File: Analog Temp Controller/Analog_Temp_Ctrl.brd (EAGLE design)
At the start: 100 x 59 mm, 110 parts, among them IC1 TL074D, IC3 LMV358MMX, IC4 ADA4522-2, J1 USB_MINI-B_SMT, Q1 TIP41C, T1 2N3904, T2 2N3906, U1 ADR01BRZ, U2 ATMEGA32U4-AU, U3 CJT1117-3.3-SOT223, U4 CJT1117-5.0-SOT223, U5 AD5272BRMZ-20, X1 CRYSTAL-3.2-2.5

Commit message: Completed Temperature Controller, Rdy for Mfg.
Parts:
- removed LED4: (no value), led:CHIPLED_0805
- removed U5: AD5272BRMZ-20, Analog Devices_By_element14_Batch_1:SOP50P490X110-10N
- added C27, C29, C32, C34, C35, C36, C37: 0.1uF, rcl:C0805
- added C28, C30, C33: 10uF, rcl:C0805
- added C31: 1uF, rcl:C0805
- added PWR: (no value), led:CHIPLED_0805
- added RADD: Radd, rcl:R0805
- added U6: AD5292BRUZ-20, Analog Devices_By_element14_Batch_1:SOP65P640X120-14N
- moved C9 8.41 mm to (91.2, 34.3), turned to 270 degrees
- moved R32 7.27 mm to (85.0, 30.0)
- moved R31 7.03 mm to (85.0, 27.7)
- moved C10 6.79 mm to (85.0, 25.4)
- moved C19 5.82 mm to (55.0, 46.6), turned to 180 degrees
- moved U1 4.02 mm to (90.2, 27.9), turned to 270 degrees
- moved R8 3.32 mm to (56.4, 24.3), turned to 270 degrees
- moved JP7 3.09 mm to (74.7, 25.7), turned to 180 degrees
- moved R36 2.51 mm to (59.2, 43.7), turned to 0 degrees
- moved C6 1.40 mm to (65.5, 22.1)
- moved R20 1.40 mm to (67.9, 22.1)
- moved R19 1.37 mm to (67.9, 17.5), turned to 90 degrees
- moved JP8 1.27 mm to (38.1, 26.2)
- moved R11 1.27 mm to (54.0, 13.6)
- moved R15 1.27 mm to (51.6, 13.6)
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- renumbered LED2 to RX, LED3 to TX
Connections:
- removed net N$52: JP8.3, U2.39
- removed net VSS: U5.4
- new net DPSS: U2.1, U6.12
- new net N$39: JP8.1, U2.40
- new net N$50: C31.2, U6.7
- net +15V: now also C27.1, C28.1, C36.2, C37.2, U6.6
- net +5V: now also C32.2, C33.2, U6.1, U6.8
- net -15V: now also C29.2, C30.2, C34.1, C35.1, U6.2
- net GND: now also C27.2, C28.2, C29.1, C30.1, C31.1, C32.1, C33.1, C34.2, C35.2, C36.1, C37.1, PWR.C, U6.9; no longer LED4.C
- net MOSI: now also U6.10
- net N$2: now also JP8.3, U2.38; no longer JP8.1, U2.41
- net N$30: now also U2.39; no longer U2.40
- net N$47: now also IC4.5, JP7.1, RADD.1; no longer U5.1, U5.7
- net N$49: now also PWR.A; no longer LED4.A
- net RA: now also U6.3; no longer U5.2
- net RW: now also RADD.2, U6.4; no longer IC4.5, JP7.1, U5.3
- net SCK: now also U6.11
- net UGBOUT: now also U2.41; no longer U2.38
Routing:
- net MOSI: track 11.1 -> 82.1 mm, vias 0 -> 2
- net SCK: track 11.7 -> 77.8 mm, vias 0 -> 2
- net DPSS: track 0.00 -> 59.6 mm, vias 0 -> 2
- net +5V: track 248.8 -> 280.3 mm, vias 6 -> 8
- net N$47: track 4.99 -> 32.9 mm, vias 0 -> 1
- net -15V: track 102.1 -> 122.8 mm, vias 4 -> 5
- net +15V: track 110.5 -> 126.7 mm, vias 4 -> 7
- net UGBOUT: track 47.5 -> 62.0 mm
- net N$52: track 9.88 -> 0.00 mm
- net RW: track 21.3 -> 12.0 mm
- net N$39: track 0.00 -> 7.52 mm
- net N$2: track 6.50 -> 10.3 mm
- net VUSB: track 74.1 -> 77.7 mm
- net N$10: track 29.9 -> 27.2 mm
- net N$50: track 0.00 -> 2.58 mm
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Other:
- board text added: "3V3"
- board text added: "SCL"
- board text added: "SDA"

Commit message: Preliminary changes to new version.
New features: Microntroller for current driver as well, seperate A/D
grounding, upgrade to ARM Cortec uC, several other improvements.
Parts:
- removed H1, H2, H3, H4: MOUNT-PAD-ROUND3.0, holes:3,0-PAD
- moved C8 2.41 mm to (82.5, 10.9)
- moved T1 2.33 mm to (87.2, 12.7)
- moved R29 1.42 mm to (82.5, 13.1), turned to 180 degrees
- moved D1 1.37 mm to (85.9, 18.4), turned to 0 degrees
- moved C7 1.25 mm to (90.3, 19.8)
- moved D2 0.92 mm to (85.9, 16.1), turned to 180 degrees
- moved C9 0.89 mm to (90.3, 34.3)
- moved C32 0.76 mm to (88.1, 34.3)
- moved U1 0.76 mm to (89.4, 27.9)
- moved C33 0.64 mm to (86.0, 34.3)
- moved T2 0.64 mm to (73.7, 3.17)
- moved C10 0.63 mm to (84.3, 25.4)
- moved R31 0.63 mm to (84.3, 27.7)
- moved R32 0.63 mm to (84.3, 30.0)
- moved R38 0.51 mm to (8.00, 26.0)
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- renumbered RADD to RA, RE to RS
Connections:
- net GND: no longer H1.B3,0, H2.B3,0, H3.B3,0, H4.B3,0
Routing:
- net N$34: track 26.4 -> 0.00 mm
- net N$22: track 29.8 -> 7.09 mm
- net N$23: track 19.8 -> 4.75 mm
- net N$31: track 21.8 -> 24.6 mm, vias 1 -> 2
- net +15V: track 126.7 -> 129.0 mm
- net N$25: track 3.94 -> 2.29 mm
- net RST: track 50.2 -> 51.2 mm
- net N$29: track 2.22 -> 2.88 mm
- net RA: track 24.2 -> 23.6 mm
- net SDA: track 15.0 -> 15.5 mm
- net SCL: track 13.6 -> 14.1 mm
- added copper zone on layer 1, net N$22
- added copper zone on layer 1, net N$23
- added copper zone on layer 1, net N$34
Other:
- board text added: "+/-15V"
- board text added: "Digital I/O"
- board text added: "I2C Header"
- board text added: "ICSP"
- board text added: "INTEGRAL GAIN"
- board text added: "NTC"
- board text added: "PRESET CURRENT"
- board text added: "PROP GAIN"
- board text added: "SUPPLY"
- board text added: "Serial"
- board text added: "TEC SUPPLY"

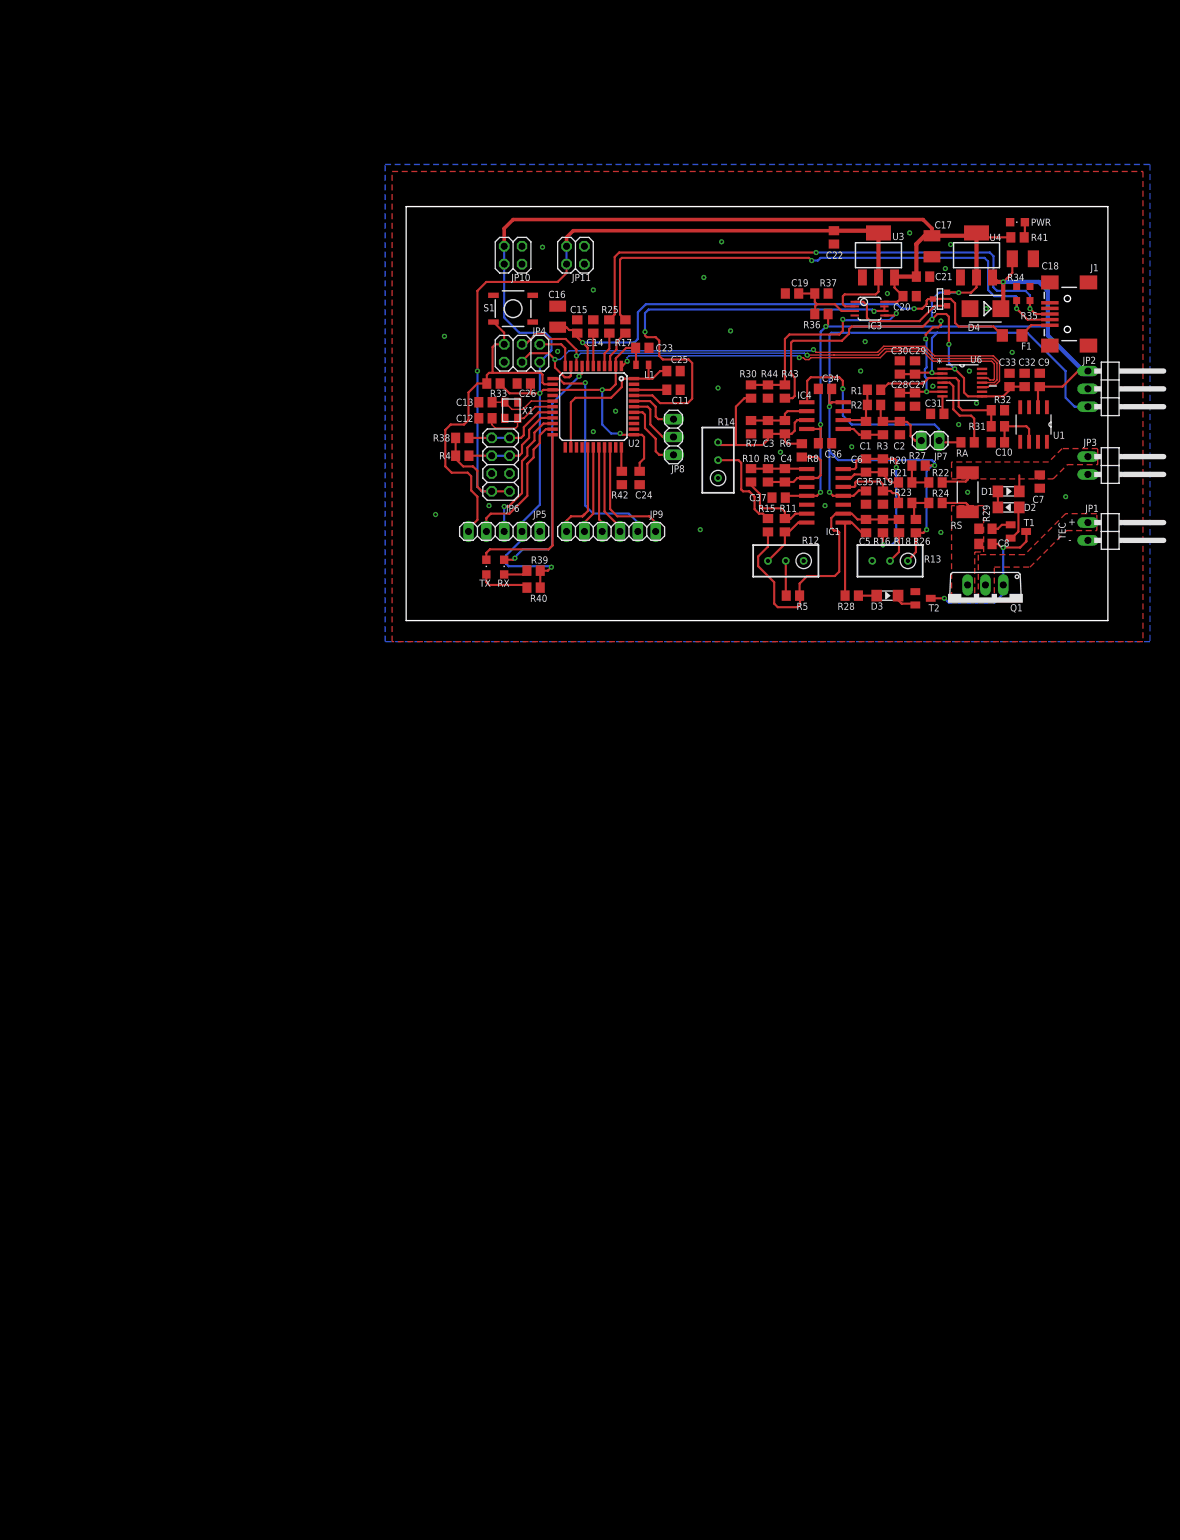
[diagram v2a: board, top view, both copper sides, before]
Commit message: Rev1.1 of CUR CTRL Complete, Ready for Mfg. Temp Ctrl WIP
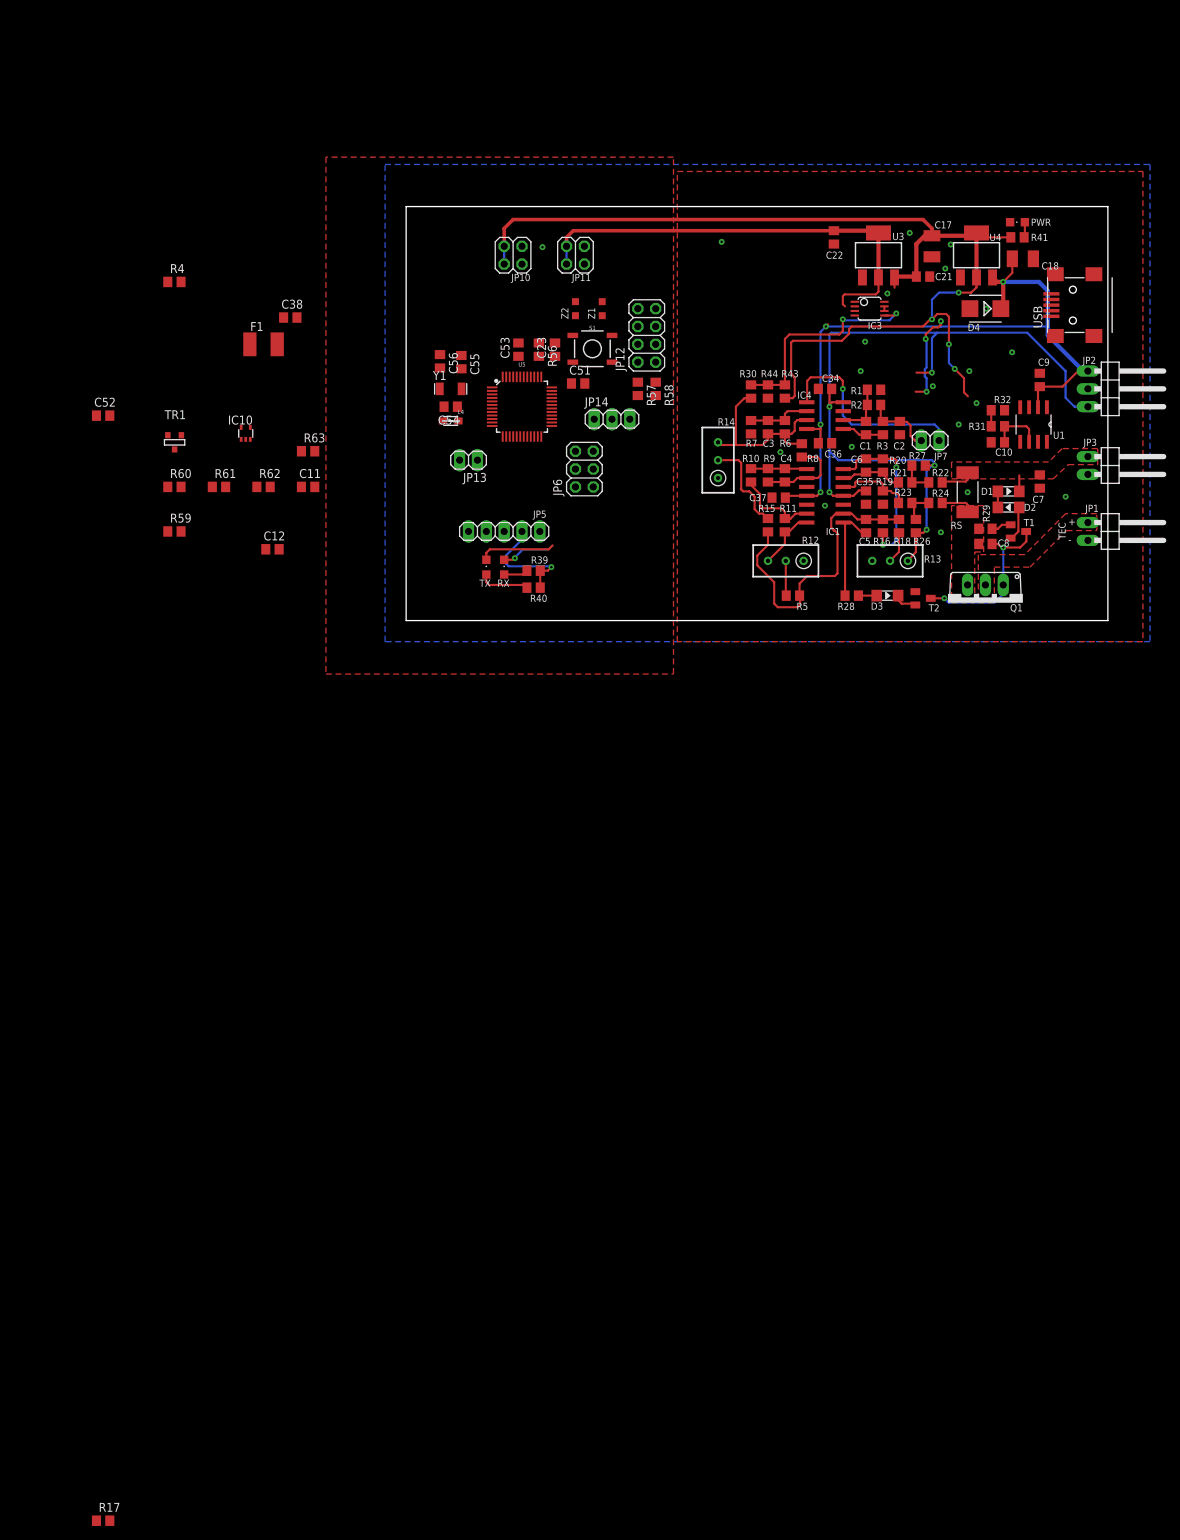
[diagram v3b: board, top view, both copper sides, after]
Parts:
- removed C13: 18pF, rcl:C0805
- removed C14, C25, C31: 1uF, rcl:C0805
- removed C15, C19, C20, C24, C26, C27, C29, C32: 0.1uF, rcl:C0805
- removed C16: 10uF, rcl:SMC_B
- removed C28, C30, C33: 10uF, rcl:C0805
- removed J1: USB_MINI-B_SMT, SparkFun-Connectors:USB-MINIB
- removed JP4: (no value), pinhead:2X03
- removed JP8: (no value), pinhead:1X03
- removed JP9: (no value), pinhead:1X06
- removed L1: MH2029-300Y, SparkFun-Coils:0805
- removed R25: 22R, rcl:R0805
- removed R33, R36, R37, R42: 10K, rcl:R0805
- removed R34, R35: CG0603MLC-05E, varistor:CT/CN0603
- removed R38: 4.7K, rcl:R0805
- removed RA: Radd, rcl:R0805
- removed T3: (no value), zetex:SOT-23
- removed U2: ATMEGA32U4-AU, adafruit:TQFP44
- removed U6: AD5292BRUZ-20, Analog Devices_By_element14_Batch_1:SOP65P640X120-14N
- removed X1: CRYSTAL-3.2-2.5, Arduino_Leonardo-REV3b:CRYSTAL-3.2-2.5
- added C38, C51, C52, C54, C55, C56: 100nF, rcl:C0805
- added C53: 1uF, rcl:C0805
- added IC10: 74LVC1G125DCKR, Arduino-M0-V1:INTEGRATEDCIRCUITS_SC70-5
- added JP12: (no value), pinhead:2X04
- added JP13: (no value), pinhead:1X02
- added JP14: (no value), pinhead:1X03
- added L4: MH2029-300Y, Arduino-M0-V1:PROTEZIONE_0805
- added R56, R63: 330R, rcl:R0805
- added R57, R58, R59: 10K, rcl:R0805
- added R60, R61, R62: 100K, rcl:R0805
- added TR1: PMV48XP, Arduino-M0-V1:TRANSISTORS_SOT-23
- added U5: ATSAMD21G-A, SparkFun-IC-Microcontroller:TQFP-48
- added USB: (no value), adafruit:USB-MINIB
- added Y1: 32,768Khz_SMD, Arduino-M0-V1:CRISTALLI_RESONATOR_EPSON_FC_145
- added Z1, Z2: BRNCG0603MLC-05E, Arduino-M0-V1:PROTEZIONE_CT/CN0603
- C11, C23: value 0.1uF -> 10nF
- C12: value 18pF -> 10uF
- F1: value 6V/0.5A -> MF-MSMF050-2 500mA; device SparkFun-Fuses:1206 -> Arduino-M0-V1:PROTEZIONE_L1812
- JP6: device pinhead:2X04 -> pinhead:2X03
- R17: value 22R -> (none)
- R4: value 4.7K -> 10K
- S1: value MOMENTARY-SWITCH-SPST-SMD-5.2MM -> MOM SWITCH
- moved R17 185.7 mm to (-43.2, -128.3), turned to 0 degrees
- moved F1 106.7 mm to (-20.3, 39.4), turned to 0 degrees
- moved C11 53.9 mm to (-14.0, 19.1)
- moved R4 47.9 mm to (-33.0, 48.3), turned to 0 degrees
- moved C12 35.6 mm to (-19.1, 10.2), turned to 0 degrees
- moved S1 12.7 mm to (26.5, 38.7)
- moved C23 12.4 mm to (21.2, 38.6), turned to 90 degrees
- moved JP6 12.0 mm to (25.4, 21.6)
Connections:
- removed net DPSS: U2.1, U6.12
- removed net MISO: JP4.1, U2.11
- removed net MOSI: JP4.4, U2.10, U6.10
- removed net N$2: JP8.3, U2.38
- removed net N$30: JP8.2, U2.39
- removed net N$32: R25.2, U2.4
- removed net N$33: J1.D-, R17.1, R34.1
- removed net N$36: C11.1, U2.42
- removed net N$37: J1.D+, R25.1, R35.1
- removed net N$38: C19.1, IC3.3, R36.1, R37.2
- removed net N$39: JP8.1, U2.40
- removed net N$40: R42.2, U2.33
- removed net N$41: F1.1, J1.VBUS
- removed net N$43: C12.1, U2.17, X1.3
- removed net N$44: C13.1, U2.16, X1.1
- removed net N$45: IC3.1, T3.3
- removed net N$47: IC4.5, JP7.1, RA.1
- removed net N$50: C31.2, U6.7
- removed net N$51: C25.2, L1.2, U2.24, U2.44
- removed net N$53: JP9.6, U2.27
- removed net N$54: JP9.1, U2.31
- removed net N$55: JP9.2, U2.12
- removed net N$56: JP9.3, U2.30
- removed net N$57: JP9.4, U2.29
- removed net N$58: JP9.5, U2.28
- removed net N$7: R17.2, U2.3
- removed net RA: R1.2, R31.1, R32.2, U6.3
- removed net SCK: JP4.3, U2.9, U6.11
- removed net VUSB: C15.2, C16.+, F1.2, T3.1, U2.7
- new net +12V: R60.2
- new net +3V3: C38.1, C51.1, C52.1, IC10.5, JP12.1, JP12.2, L4.2, R4.2, R57.2, R58.2, R62.2, U5.17, U5.36, U5.44
- new net CS_DAC: U5.24
- new net DCURMON: U5.8
- new net DGND: C11.2, C12.1, C23.2, C38.2, C51.2, C52.2, C53.2, C54.2, C55.1, C56.1, IC10.3, JP12.3, JP12.4, JP6.6, R59.1, R61.1, S1.1, U5.18, U5.35, U5.42, U5.5, USB.GND, Z1.2, Z2.2
- new net ENCA: U5.14
- new net ENCB: U5.13
- new net ENCBTN: U5.15
- new net MOSI_DAC: U5.22
- new net N$18: C54.1, L4.1, U5.6
- new net N$52: C55.2, U5.1, Y1.P$2
- new net N$59: C56.2, U5.2, Y1.P$1
- new net N$60: U5.7
- new net N$61: JP14.3, U5.30
- new net N$62: JP14.2, U5.29
- new net N$63: JP14.1, U5.28
- new net PA02_AIN0: U5.3
- new net PA04_AIN4: JP13.2, U5.9
- new net PA05_AIN5: JP13.1, U5.10
- new net PA28_USB_HOST_EN: R63.1, U5.41
- new net PB10_S4_SPI_MOSI: JP6.4, U5.19
- new net PB11_S4_SPI_SCK: JP6.3, U5.20
- new net PB12_S4_SPI_MISO: JP6.1, U5.21
- new net RESET: JP6.5, R4.1, R56.1, S1.3
- new net SCK_DAC: U5.23
- new net TARGET_RESET: C23.1, R56.2, U5.40
- new net TARGET_USB_N: U5.33, USB.D-, Z1.1
- new net TARGET_USB_P: U5.34, USB.D+, Z2.1
- new net USBVCC: C12.2, F1.2, R59.2, TR1.1
- new net USB_ID: IC10.1, IC10.2, R62.1, R63.2, USB.ID
- new net V+: IC3.8
- new net V-: IC3.4
- new net VDDCORE: C53.1, U5.43
- new net VIN: U5.47
- new net VREG: R1.2, R17.1, R31.1, R32.2
- new net XUSB: C11.1, F1.1, USB.VBUS
- net +15V: no longer C27.1, C28.1, R36.2, U6.6
- net +5V: now also JP6.2, TR1.2; no longer C20.1, C23.2, C24.2, C26.2, C32.2, C33.2, IC3.8, JP4.2, L1.1, R33.2, T3.2, U2.14, U2.2, U2.34, U6.1, U6.8
- net -15V: no longer C29.2, C30.2, U6.2
- net 3V3: no longer IC3.2, JP6.1, JP6.2, R38.2, R4.2
- net GND: no longer C11.2, C12.2, C13.2, C14.1, C15.1, C16.-, C19.2, C20.2, C23.1, C24.1, C25.1, C26.1, C27.2, C28.2, C29.1, C30.1, C31.1, C32.1, C33.1, IC3.4, J1.GND, J1.S1, J1.S2, J1.S3, J1.S4, JP4.6, JP6.3, JP6.4, R34.2, R35.2, R37.1, R42.1, S1.1, U2.15, U2.23, U2.35, U2.43, U2.5, U6.9, X1.2, X1.4
- net N$46: now also IC10.4, R60.1, R61.2, TR1.3; no longer C14.2, U2.6
- net RST: no longer JP4.5, R33.1, S1.3, U2.13
- net RW: now also IC4.5, JP7.1, R17.2; no longer RA.2, U6.4
- net RXD: no longer U2.20
- net RXLED: no longer U2.8
- net SCL: now also JP12.7, JP12.8, R58.1, U5.32; no longer JP6.7, JP6.8, R38.1, U2.18
- net SDA: now also JP12.5, JP12.6, R57.1, U5.31; no longer JP6.5, JP6.6, R4.1, U2.19
- net TXD: no longer U2.21
- net TXLED: no longer U2.22
- net UGBOUT: no longer U2.41
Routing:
- net +5V: track 279.8 -> 172.6 mm, vias 8 -> 5
- net MOSI: track 82.1 -> 0.00 mm, vias 2 -> 0
- net N$37: track 80.1 -> 0.00 mm, vias 2 -> 0
- net N$33: track 79.2 -> 0.00 mm, vias 2 -> 0
- net SCK: track 77.8 -> 0.00 mm, vias 2 -> 0
- net VUSB: track 77.7 -> 0.00 mm, vias 2 -> 0
- net UGBOUT: track 62.0 -> 0.65 mm, vias 2 -> 0
- net 3V3: track 124.7 -> 64.1 mm, vias 1 -> 0
- net DPSS: track 59.6 -> 0.00 mm, vias 2 -> 0
- net RST: track 51.2 -> 0.00 mm
- net N$47: track 32.9 -> 0.00 mm, vias 1 -> 0
- net N$55: track 32.3 -> 0.00 mm, vias 1 -> 0
- net RXLED: track 35.1 -> 7.76 mm, vias 2 -> 1
- net N$51: track 24.4 -> 0.00 mm
- net RA: track 23.6 -> 0.00 mm
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- added copper zone on layer 1, net DGND
